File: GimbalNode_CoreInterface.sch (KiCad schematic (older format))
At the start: 1 part

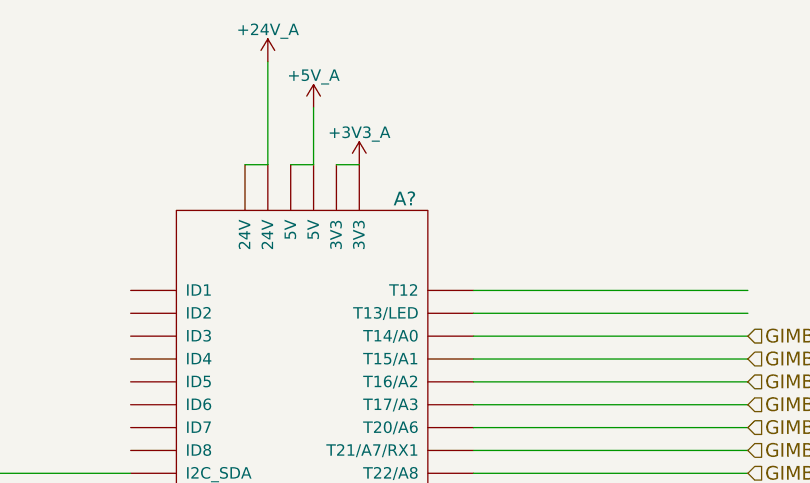
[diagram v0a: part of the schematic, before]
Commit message: Fixup various caps on 4-20ma sheet.
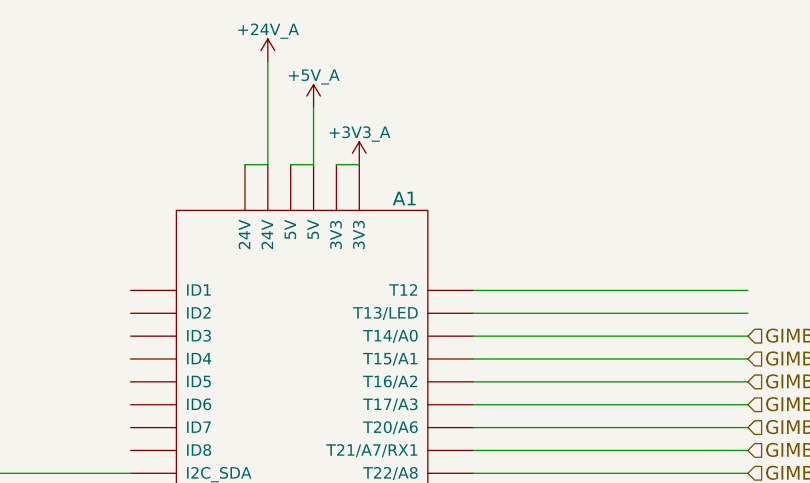
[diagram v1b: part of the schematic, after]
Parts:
- gave numbers to parts that had none: 1
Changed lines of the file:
@@
 GIMBAL_STEP_ENA
 $Comp
-L +3V3_A #PWR?
+L +3V3_A #PWR01
 U 1 1 575833F8
 P 8400 3050
-F 0 "#PWR?" H 8400 2900 50  0001 C CNN
+F 0 "#PWR01" H 8400 2900 50  0001 C CNN
 F 1 "+3V3_A" H 8400 3190 50  0000 C CNN
 F 2 "" H 8400 3050 60  0000 C CNN
@@
 $EndComp
 $Comp
-L +5V_A #PWR?
+L +5V_A #PWR02
 U 1 1 575833F9
 P 8200 2800
-F 0 "#PWR?" H 8200 2650 50  0001 C CNN
+F 0 "#PWR02" H 8200 2650 50  0001 C CNN
 F 1 "+5V_A" H 8200 2940 50  0000 C CNN
 F 2 "" H 8200 2800 60  0000 C CNN
@@
 $EndComp
 $Comp
-L +24V_A #PWR?
+L +24V_A #PWR03
 U 1 1 575833FA
 P 8000 2600
-F 0 "#PWR?" H 8000 2450 50  0001 C CNN
+F 0 "#PWR03" H 8000 2450 50  0001 C CNN
 F 1 "+24V_A" H 8000 2740 50  0000 C CNN
 F 2 "" H 8000 2600 60  0000 C CNN
@@
 	8300 3050 8400 3050
 $Comp
-L GNDD #PWR?
+L GNDD #PWR04
 U 1 1 575833FB
 P 8250 6300
-F 0 "#PWR?" H 8250 6050 50  0001 C CNN
+F 0 "#PWR04" H 8250 6050 50  0001 C CNN
 F 1 "GNDD" H 8250 6150 50  0000 C CNN
 F 2 "" H 8250 6300 50  0000 C CNN
@@
 	7400 5400 6200 5400
 $Comp
-L NODE_CORE_CONNECTOR A?
+L NODE_CORE_CONNECTOR A1
 U 1 1 57583394
 P 8150 4600
-F 0 "A?" H 8600 6000 60  0000 C CNN
+F 0 "A1" H 8600 6000 60  0000 C CNN
 F 1 "NODE_CORE_CONNECTOR" H 8850 3050 60  0000 C CNN
 F 2 "" H 8150 4600 60  0000 C CNN

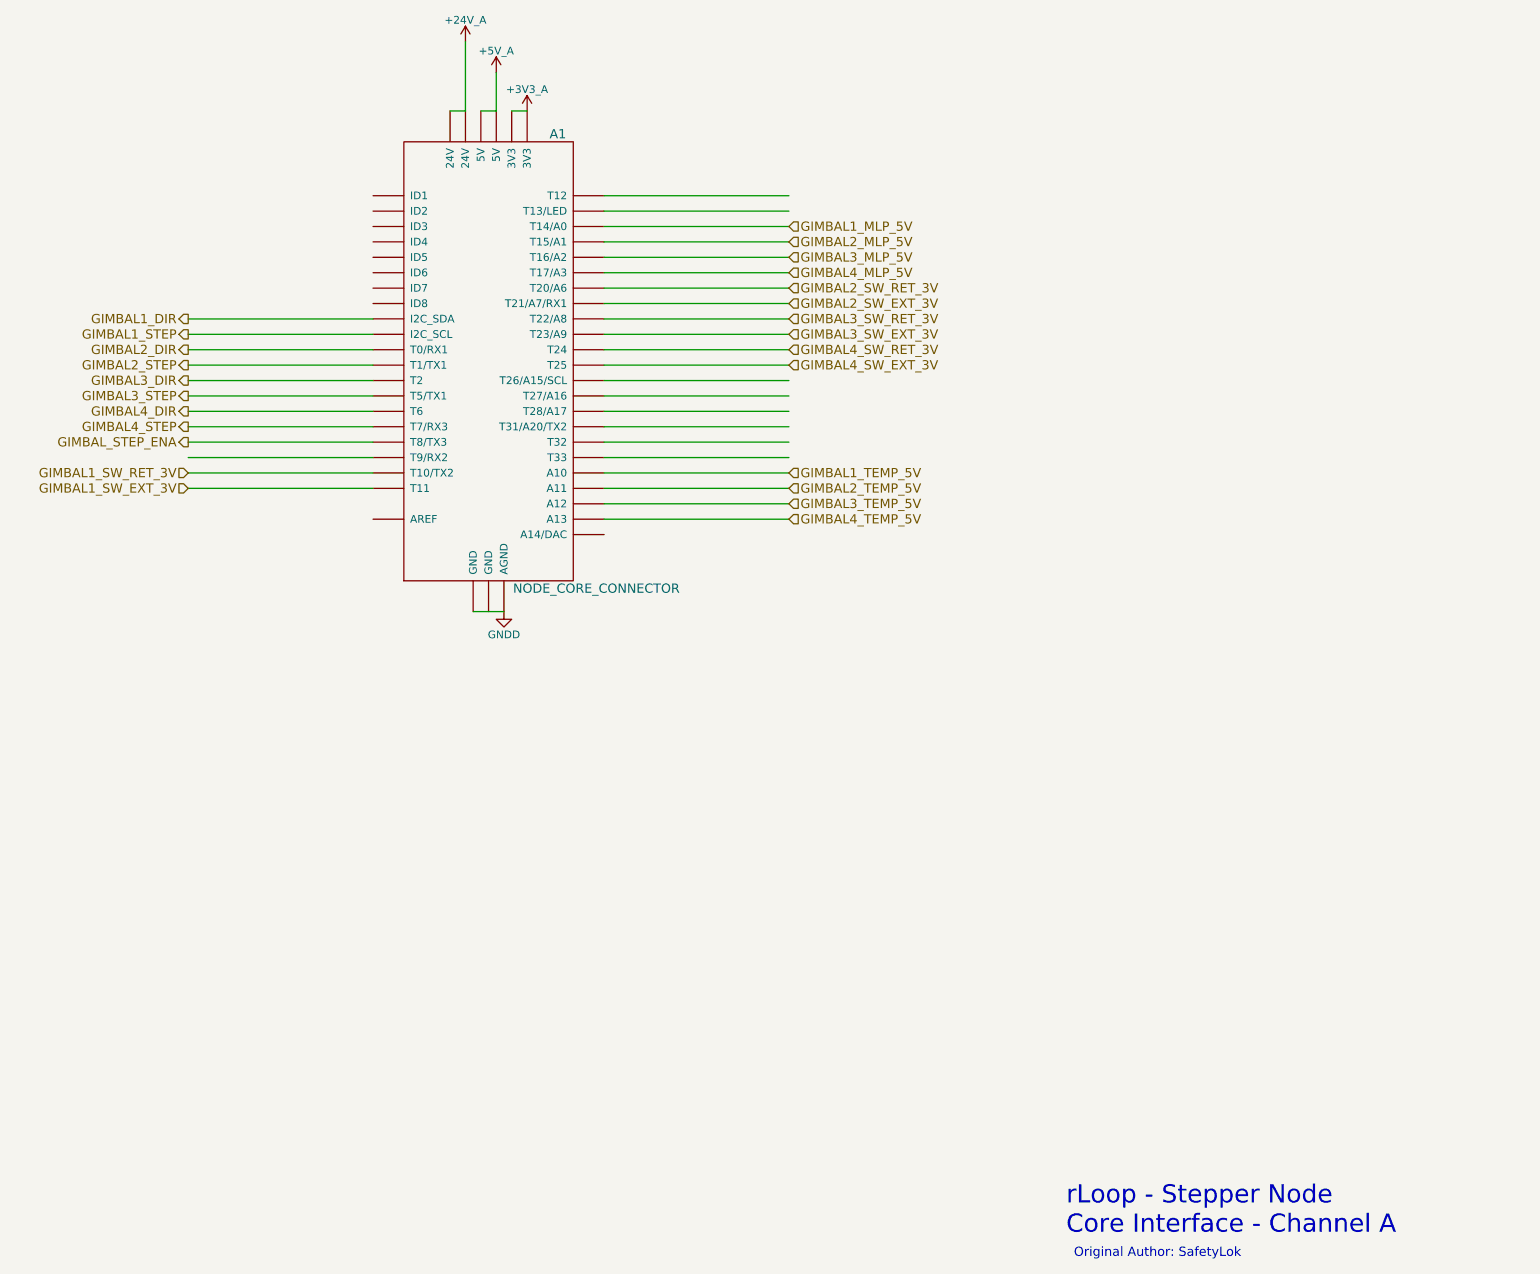
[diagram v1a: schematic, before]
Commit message: Fixup 5V to 3V connections
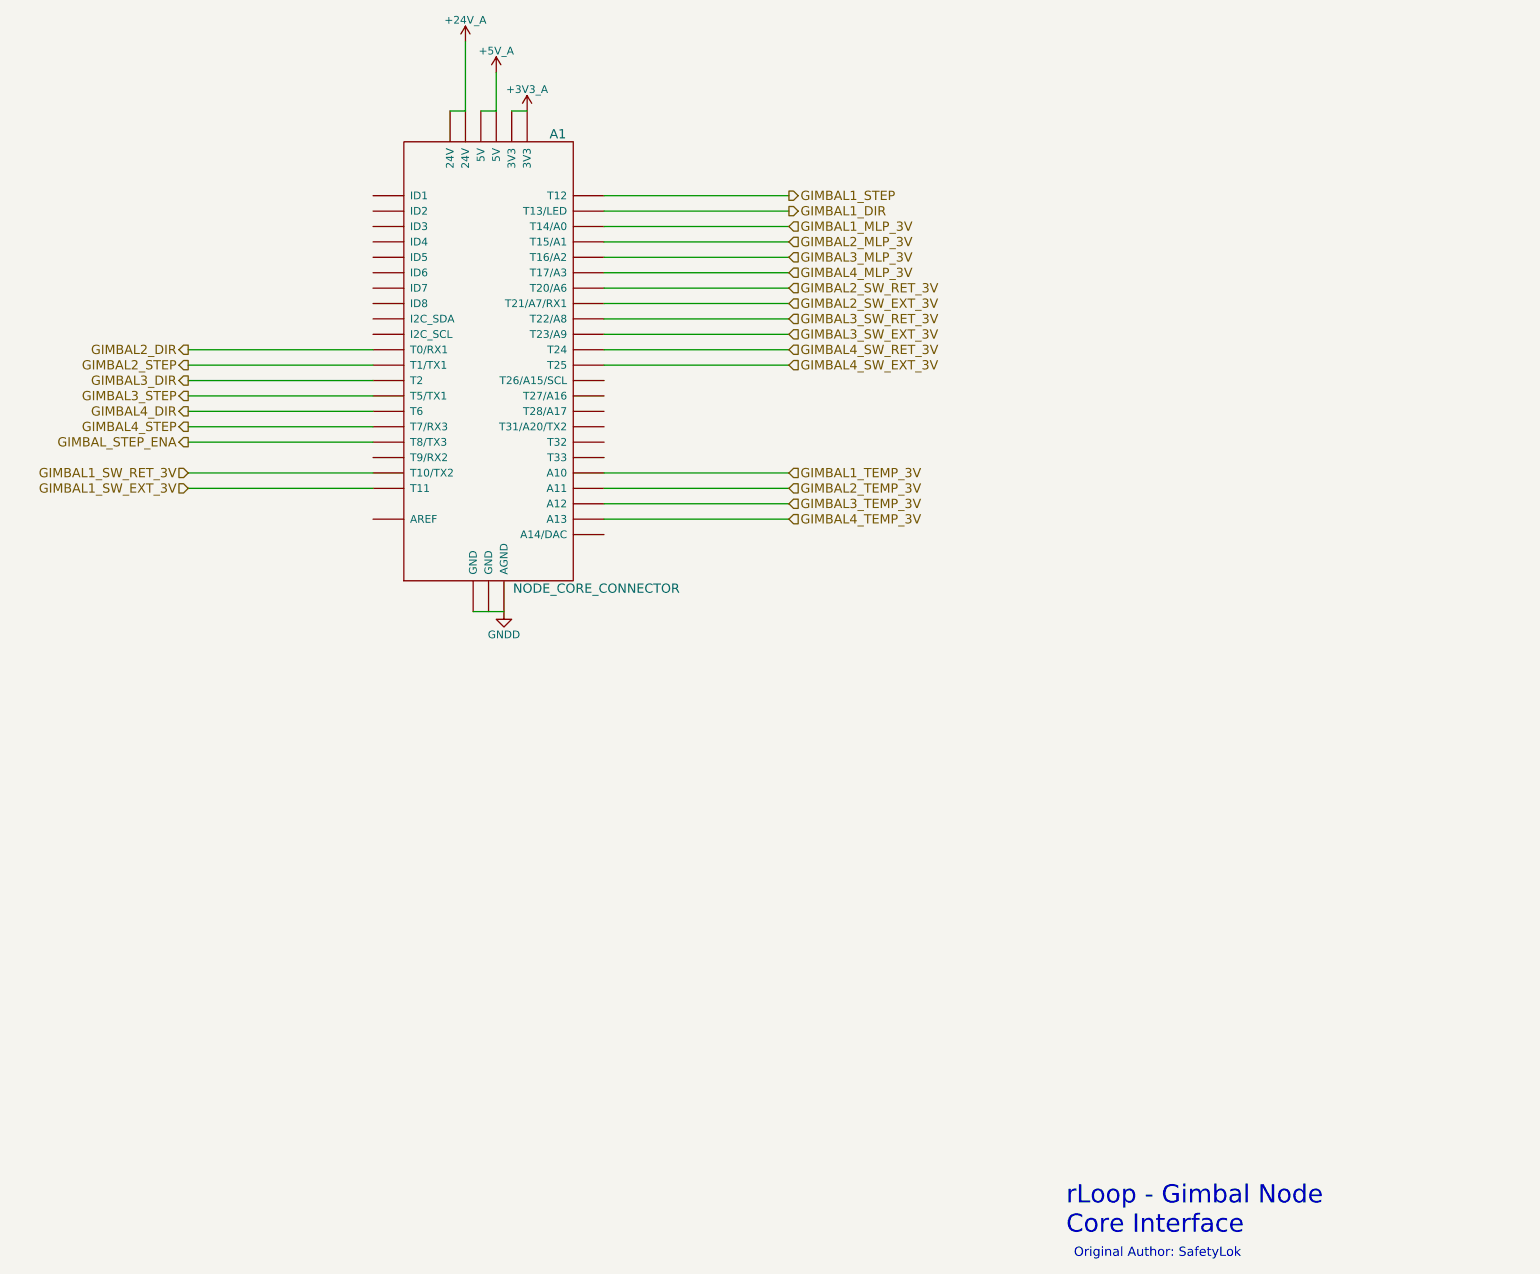
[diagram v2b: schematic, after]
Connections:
- net labels added: GIMBAL1_MLP_3V, GIMBAL1_TEMP_3V, GIMBAL2_MLP_3V, GIMBAL2_TEMP_3V, GIMBAL3_MLP_3V, GIMBAL3_TEMP_3V, GIMBAL4_MLP_3V, GIMBAL4_TEMP_3V
- net labels removed: GIMBAL1_MLP_5V, GIMBAL1_TEMP_5V, GIMBAL2_MLP_5V, GIMBAL2_TEMP_5V, GIMBAL3_MLP_5V, GIMBAL3_TEMP_5V, GIMBAL4_MLP_5V, GIMBAL4_TEMP_5V
- wire segments 40 -> 31
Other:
- note added: "rLoop - Gimbal Node\nCore Interface"
- note removed: "rLoop - Stepper Node\nCore Interface - Channel A"
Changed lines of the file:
@@
 $EndDescr
 Text Notes 11900 10350 0    118  ~ 0
-rLoop - Stepper Node\nCore Interface - Channel A
+rLoop - Gimbal Node\nCore Interface
 Text Notes 11950 10500 0    60   ~ 0
 Original Author: SafetyLok
-Text HLabel 6200 4400 0    60   Output ~ 0
-GIMBAL1_DIR
-Text HLabel 6200 4500 0    60   Output ~ 0
-GIMBAL1_STEP
 Text HLabel 6200 4600 0    60   Output ~ 0
 GIMBAL2_DIR
@@
 GIMBAL_STEP_ENA
 $Comp
-L +3V3_A #PWR01
+L +3V3_A #PWR4
 U 1 1 575833F8
 P 8400 3050
-F 0 "#PWR01" H 8400 2900 50  0001 C CNN
+F 0 "#PWR4" H 8400 2900 50  0001 C CNN
 F 1 "+3V3_A" H 8400 3190 50  0000 C CNN
 F 2 "" H 8400 3050 60  0000 C CNN
@@
 $EndComp
 $Comp
-L +5V_A #PWR02
+L +5V_A #PWR2
 U 1 1 575833F9
 P 8200 2800
-F 0 "#PWR02" H 8200 2650 50  0001 C CNN
+F 0 "#PWR2" H 8200 2650 50  0001 C CNN
 F 1 "+5V_A" H 8200 2940 50  0000 C CNN
 F 2 "" H 8200 2800 60  0000 C CNN
@@
 $EndComp
 $Comp
-L +24V_A #PWR03
+L +24V_A #PWR1
 U 1 1 575833FA
 P 8000 2600
-F 0 "#PWR03" H 8000 2450 50  0001 C CNN
+F 0 "#PWR1" H 8000 2450 50  0001 C CNN
 F 1 "+24V_A" H 8000 2740 50  0000 C CNN
 F 2 "" H 8000 2600 60  0000 C CNN
@@
 	8300 3050 8400 3050
 $Comp
-L GNDD #PWR04
+L GNDD #PWR3
 U 1 1 575833FB
 P 8250 6300
-F 0 "#PWR04" H 8250 6050 50  0001 C CNN
+F 0 "#PWR3" H 8250 6050 50  0001 C CNN
 F 1 "GNDD" H 8250 6150 50  0000 C CNN
 F 2 "" H 8250 6300 50  0000 C CNN
@@
 Wire Wire Line
 	8050 6300 8250 6300
-Wire Wire Line
-	7400 4400 6200 4400
-Wire Wire Line
-	7400 4500 6200 4500
 Wire Wire Line
 	7400 4600 6200 4600
@@
 	10100 4600 8900 4600
 Wire Wire Line
-	10100 5100 8900 5100
-Wire Wire Line
-	10100 5200 8900 5200
-Wire Wire Line
-	10100 5300 8900 5300
-Wire Wire Line
 	10100 4700 8900 4700
-Wire Wire Line
-	10100 4800 8900 4800
-Wire Wire Line
-	10100 4900 8900 4900
-Wire Wire Line
-	10100 5000 8900 5000
 Wire Wire Line
 	10100 5500 8900 5500
@@
 	7400 5200 6200 5200
 Wire Wire Line
-	7400 5300 6200 5300
-Wire Wire Line
 	7400 5400 6200 5400
 $Comp
@@
 $EndComp
 Text HLabel 10100 3800 2    60   Input ~ 0
-GIMBAL1_MLP_5V
+GIMBAL1_MLP_3V
 Text HLabel 10100 3900 2    60   Input ~ 0
-GIMBAL2_MLP_5V
+GIMBAL2_MLP_3V
 Text HLabel 10100 4000 2    60   Input ~ 0
-GIMBAL3_MLP_5V
+GIMBAL3_MLP_3V
 Text HLabel 10100 4100 2    60   Input ~ 0
-GIMBAL4_MLP_5V
+GIMBAL4_MLP_3V
 Text HLabel 6200 5400 0    60   Input ~ 0
 GIMBAL1_SW_RET_3V
@@
 GIMBAL4_SW_EXT_3V
 Text HLabel 10100 5600 2    60   Input ~ 0
-GIMBAL3_TEMP_5V
+GIMBAL3_TEMP_3V
 Text HLabel 10100 5500 2    60   Input ~ 0
-GIMBAL2_TEMP_5V
+GIMBAL2_TEMP_3V
 Text HLabel 10100 5400 2    60   Input ~ 0
-GIMBAL1_TEMP_5V
+GIMBAL1_TEMP_3V
 Text HLabel 10100 5700 2    60   Input ~ 0
-GIMBAL4_TEMP_5V
+GIMBAL4_TEMP_3V
+Text HLabel 10100 3700 2    60   Output ~ 0
+GIMBAL1_DIR
+Text HLabel 10100 3600 2    60   Output ~ 0
+GIMBAL1_STEP
 $EndSCHEMATC

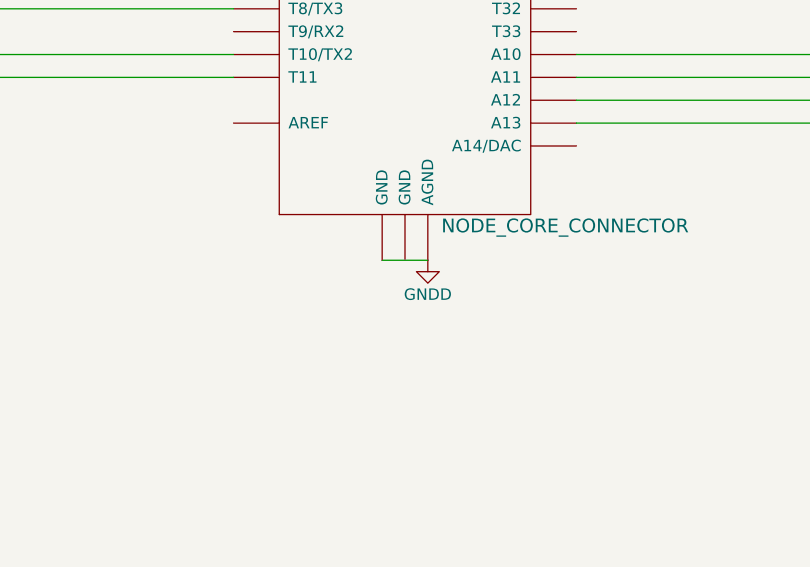
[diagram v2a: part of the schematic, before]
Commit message: Update connectors, diodes, add zener's and anotate.
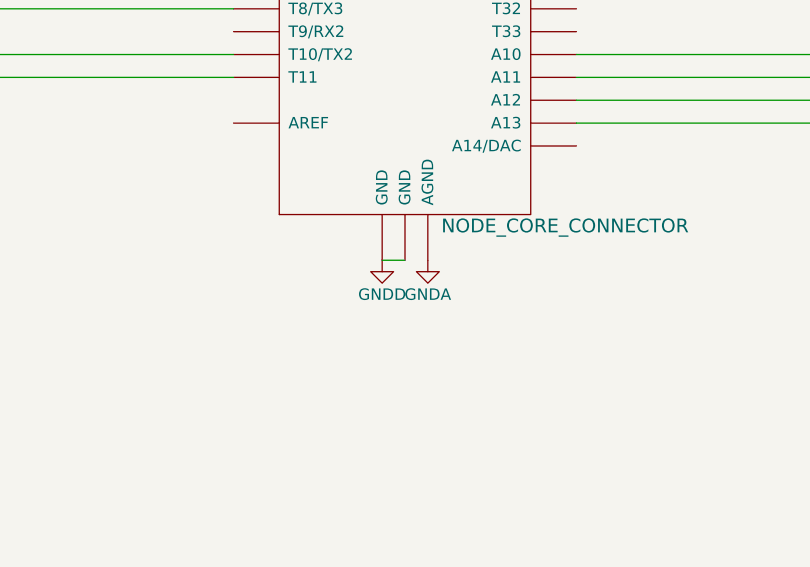
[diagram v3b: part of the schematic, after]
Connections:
- net GNDD: no longer A1.AGND
- new net GNDA: A1.AGND
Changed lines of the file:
@@
 GIMBAL_STEP_ENA
 $Comp
-L +3V3_A #PWR4
+L +3V3_A #PWR01
 U 1 1 575833F8
 P 8400 3050
-F 0 "#PWR4" H 8400 2900 50  0001 C CNN
+F 0 "#PWR01" H 8400 2900 50  0001 C CNN
 F 1 "+3V3_A" H 8400 3190 50  0000 C CNN
 F 2 "" H 8400 3050 60  0000 C CNN
@@
 $EndComp
 $Comp
-L +5V_A #PWR2
+L +5V_A #PWR02
 U 1 1 575833F9
 P 8200 2800
-F 0 "#PWR2" H 8200 2650 50  0001 C CNN
+F 0 "#PWR02" H 8200 2650 50  0001 C CNN
 F 1 "+5V_A" H 8200 2940 50  0000 C CNN
 F 2 "" H 8200 2800 60  0000 C CNN
@@
 $EndComp
 $Comp
-L +24V_A #PWR1
+L +24V_A #PWR03
 U 1 1 575833FA
 P 8000 2600
-F 0 "#PWR1" H 8000 2450 50  0001 C CNN
+F 0 "#PWR03" H 8000 2450 50  0001 C CNN
 F 1 "+24V_A" H 8000 2740 50  0000 C CNN
 F 2 "" H 8000 2600 60  0000 C CNN
@@
 	8300 3050 8400 3050
 $Comp
-L GNDD #PWR3
+L GNDD #PWR04
 U 1 1 575833FB
-P 8250 6300
-F 0 "#PWR3" H 8250 6050 50  0001 C CNN
-F 1 "GNDD" H 8250 6150 50  0000 C CNN
-F 2 "" H 8250 6300 50  0000 C CNN
-F 3 "" H 8250 6300 50  0000 C CNN
-	1    8250 6300
+P 8050 6300
+F 0 "#PWR04" H 8050 6050 50  0001 C CNN
+F 1 "GNDD" H 8050 6150 50  0000 C CNN
+F 2 "" H 8050 6300 50  0000 C CNN
+F 3 "" H 8050 6300 50  0000 C CNN
+	1    8050 6300
 	1    0    0    -1
 $EndComp
-Wire Wire Line
-	8050 6300 8250 6300
 Wire Wire Line
 	7400 4600 6200 4600
@@
 Text HLabel 10100 3600 2    60   Output ~ 0
 GIMBAL1_STEP
+Wire Wire Line
+	8150 6300 8050 6300
+$Comp
+L GNDA #PWR05
+U 1 1 575C01AC
+P 8250 6300
+F 0 "#PWR05" H 8250 6050 50  0001 C CNN
+F 1 "GNDA" H 8250 6150 50  0000 C CNN
+F 2 "" H 8250 6300 50  0000 C CNN
+F 3 "" H 8250 6300 50  0000 C CNN
+	1    8250 6300
+	1    0    0    -1
+$EndComp
 $EndSCHEMATC
